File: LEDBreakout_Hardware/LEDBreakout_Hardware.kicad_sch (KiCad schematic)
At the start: 17 parts

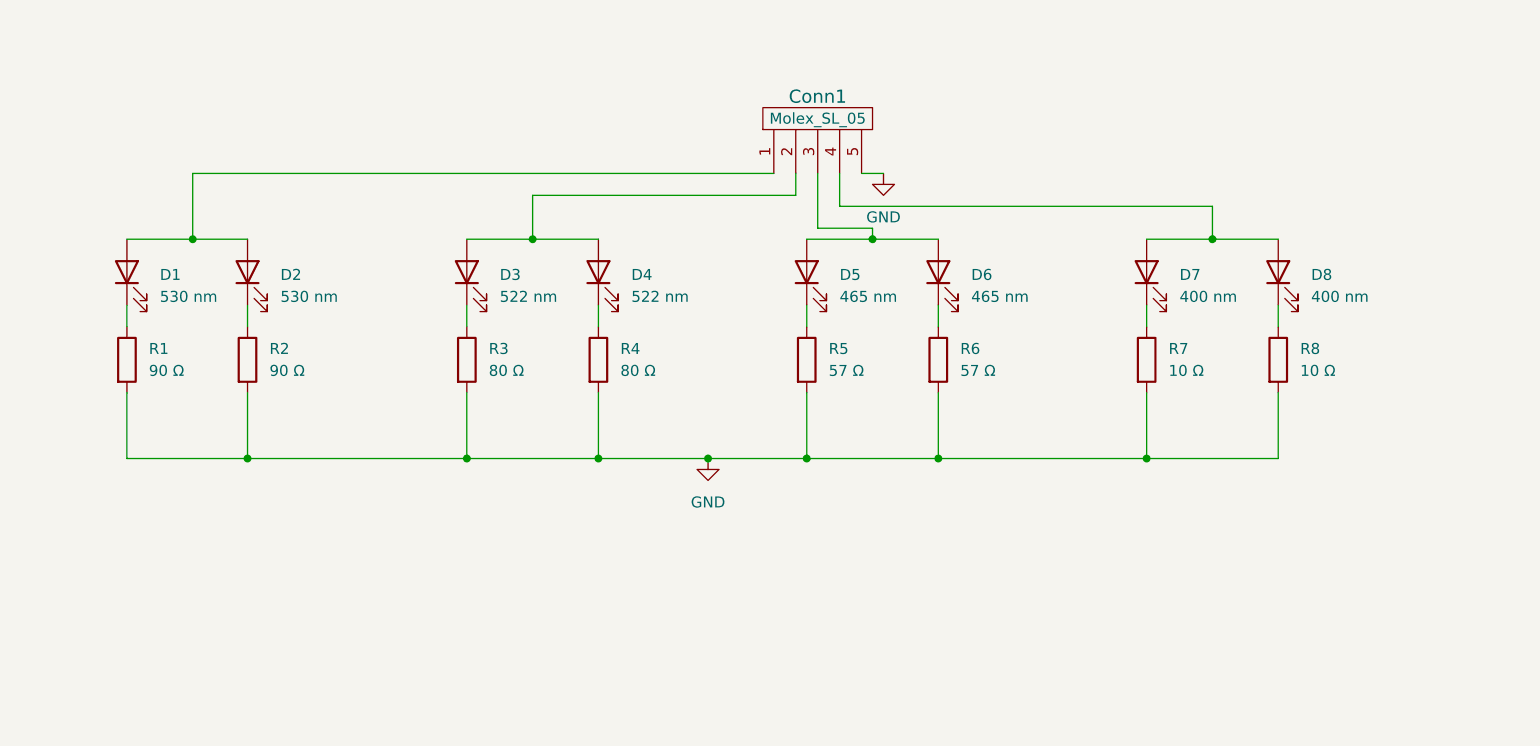
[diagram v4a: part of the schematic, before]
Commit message: Added 5V to LED connectors
Also added FETs to LEDs on breakout.
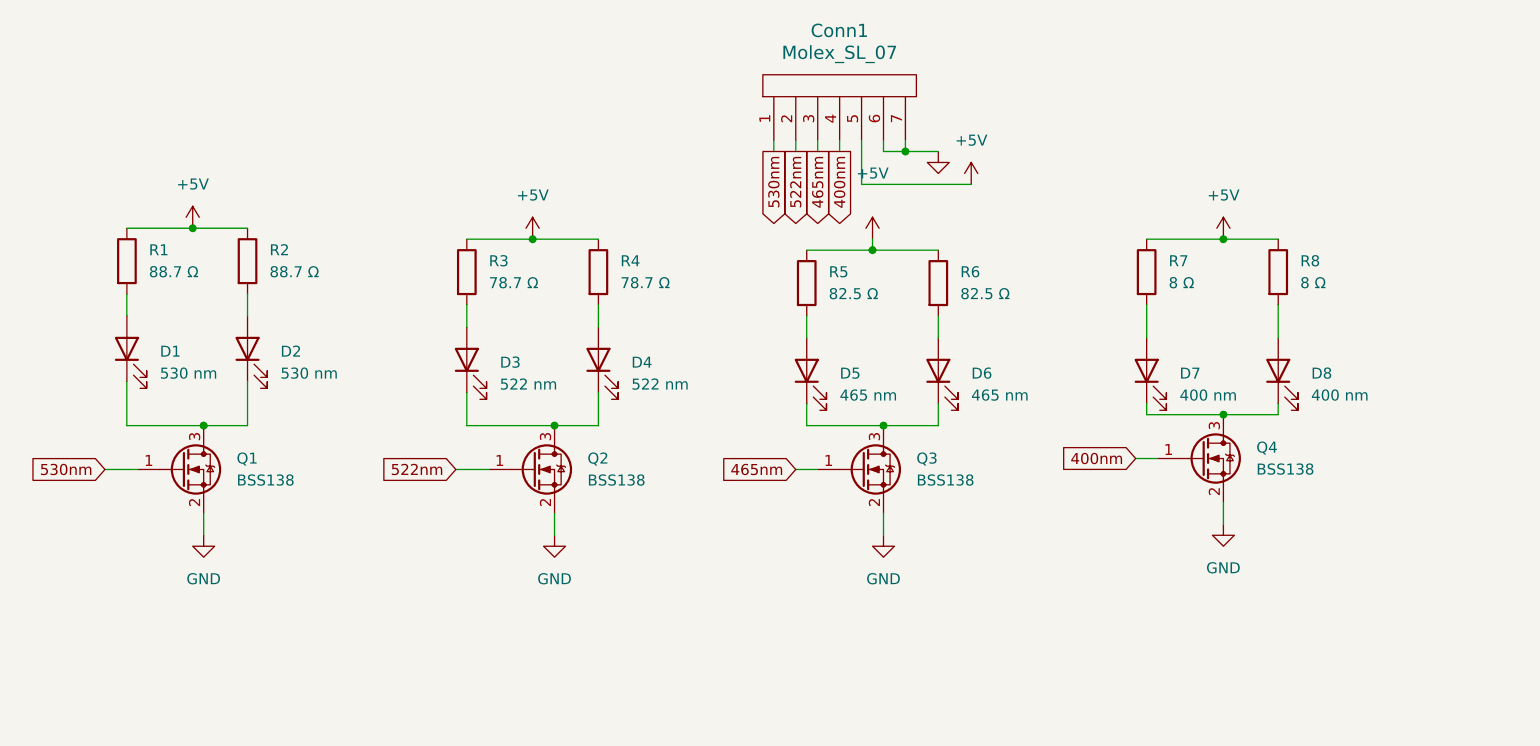
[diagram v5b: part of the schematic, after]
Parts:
- removed Conn1: Molex_SL_05, MRDT_Connectors:MOLEX_SL_05_Vertical, symbol MRDT_Connectors:Molex_SL_05
- added Conn1: Molex_SL_07, MRDT_Connectors:MOLEX_SL_07_Vertical, symbol MRDT_Connectors:Molex_SL_07
- added Q1, Q2, Q3, Q4: BSS138, Package_TO_SOT_SMD:SOT-23, symbol Transistor_FET:BSS138
- R1, R2: value 90 Ω -> 88.7 Ω
- R3, R4: value 80 Ω -> 78.7 Ω
- R5, R6: value 57 Ω -> 82.5 Ω
- R7, R8: value 10 Ω -> 8 Ω; footprint Resistor_SMD:R_0603_1608Metric_Pad0.98x0.95mm_HandSolder -> Resistor_SMD:R_2010_5025Metric_Pad1.40x2.65mm_HandSolder
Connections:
- net GND: now also Conn1.6, Conn1.7, Q1.2 (S), Q2.2 (S), Q3.2 (S), Q4.2 (S); no longer R1.2, R2.2, R3.2, R4.2, R5.2, R6.2, R7.2, R8.2
- net at D5.1 (K): now also D6.1 (K), Q3.3 (D); no longer R5.1
- net at D5.2 (A): now also R5.2; no longer D6.2 (A)
- net at D7.1 (K): now also D8.1 (K), Q4.3 (D); no longer R7.1
- net at D3.1 (K): now also D4.1 (K), Q2.3 (D); no longer R3.1
- net at D7.2 (A): now also R7.2; no longer D8.2 (A)
- net +5V: now reaches R6.1
- net +5V: now also R1.1, R2.1, R3.1, R4.1, R5.1, R7.1, R8.1, Conn1.5; no longer D6.1 (K)
- net at D2.2 (A): now also R2.2; no longer D1.2 (A)
- net at D3.2 (A): now also R3.2; no longer D4.2 (A)
- net at D2.1 (K): now also D1.1 (K), Q1.3 (D); no longer R2.1
- new net: D6.2 (A), R6.2
- new net: D8.2 (A), R8.2
- new net: D4.2 (A), R4.2
- new net: D1.2 (A), R1.2
- new net 400nm: Conn1.4, Q4.1 (G)
- new net 465nm: Conn1.3, Q3.1 (G)
- new net 522nm: Conn1.2, Q2.1 (G)
- new net 530nm: Conn1.1, Q1.1 (G)
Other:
- moved on the sheet: D1, D2, D3, D4, D5, D6, D7, D8, R1, R2, R3, R4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

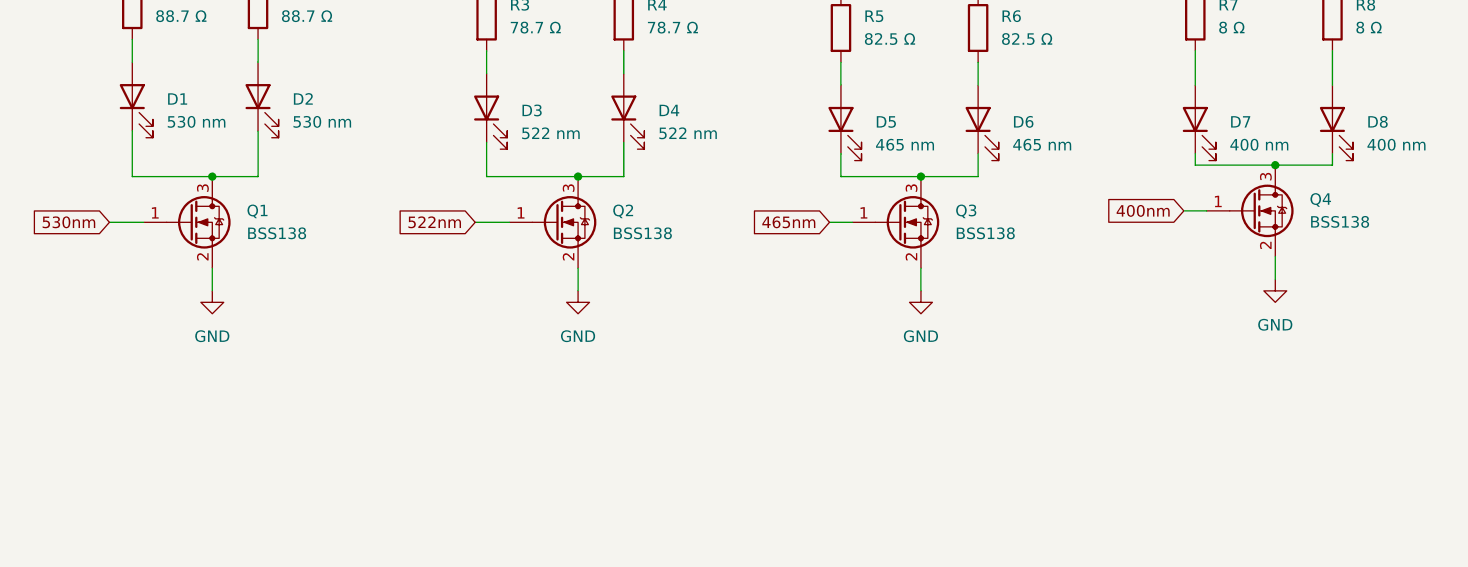
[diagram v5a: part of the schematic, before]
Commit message: Added Pull Down Resistors to MOSFETs
And some other things
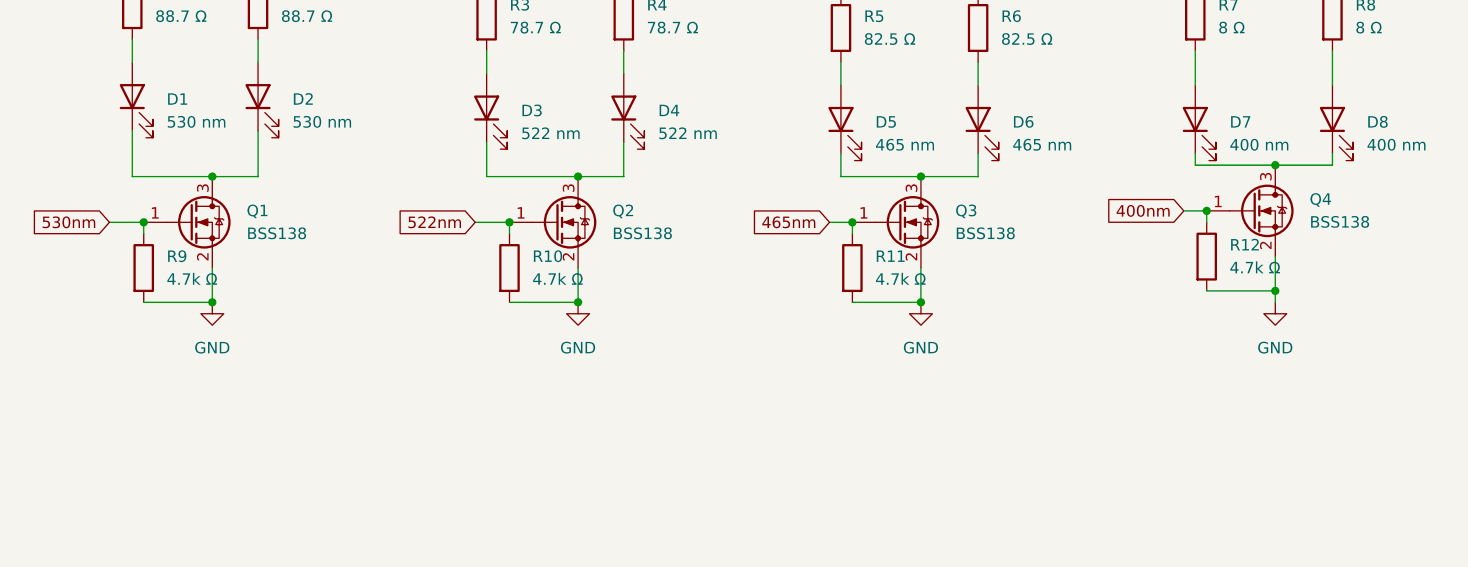
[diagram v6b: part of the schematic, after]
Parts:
- added R10, R11, R12, R9: 4.7k Ω, Resistor_SMD:R_0603_1608Metric_Pad0.98x0.95mm_HandSolder, symbol Device:R
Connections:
- net 400nm: now also R12.1
- net 465nm: now also R11.1
- net 522nm: now also R10.1
- net 530nm: now also R9.1
- net GND: now also R10.2, R11.2, R12.2, R9.2
